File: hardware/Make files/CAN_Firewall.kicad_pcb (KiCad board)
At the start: 2 copper layers, 46.3 x 18.8 mm, 31 parts, among them IC1 ATXMEGA128A4U-M, J1 DB9, J2 DB9, U1 MCP2551-I/SN, U2 MCP2551-I/SN, U3 MC78M05CDT, U4 TLV70033DDC, U5 PESDxL5UY

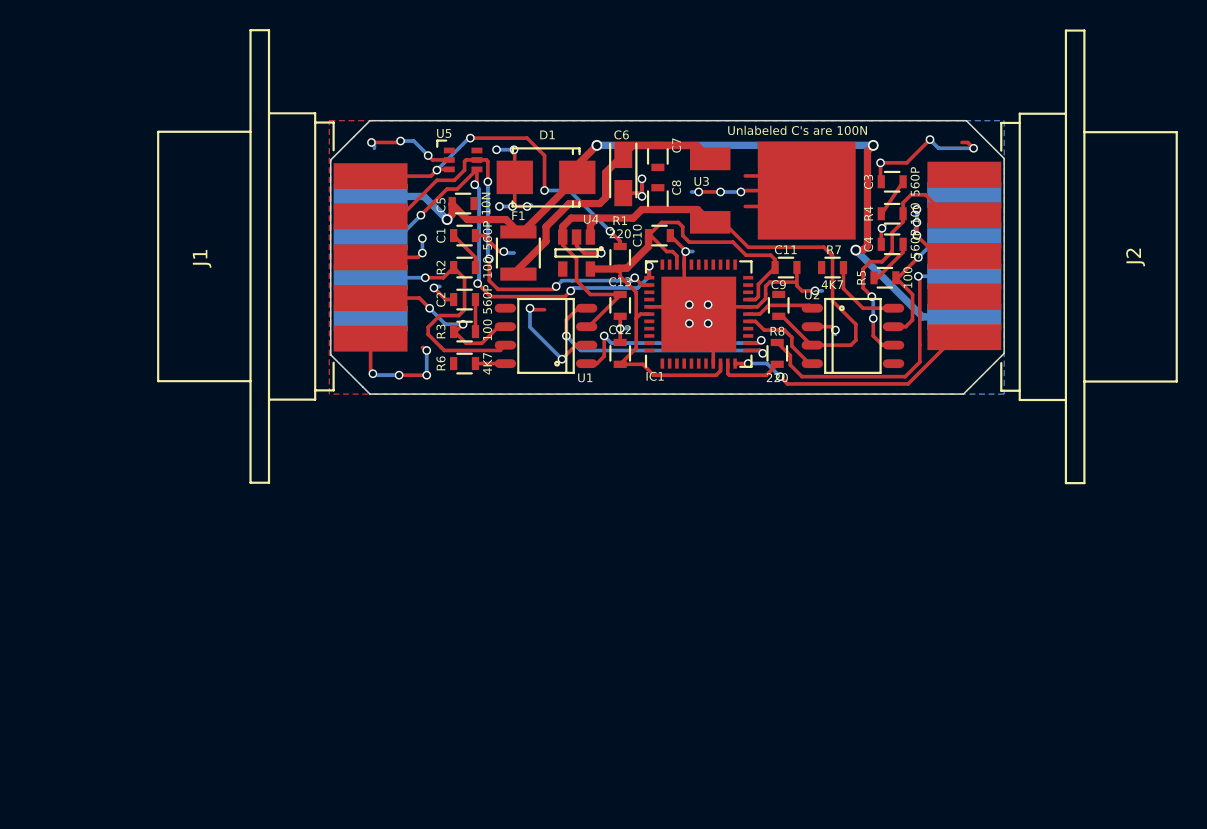
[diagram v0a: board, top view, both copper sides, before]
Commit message: V1.1 Devlopment
Created teh V1.1 hardware files. The Hardware patch for V1 will follow
this design.
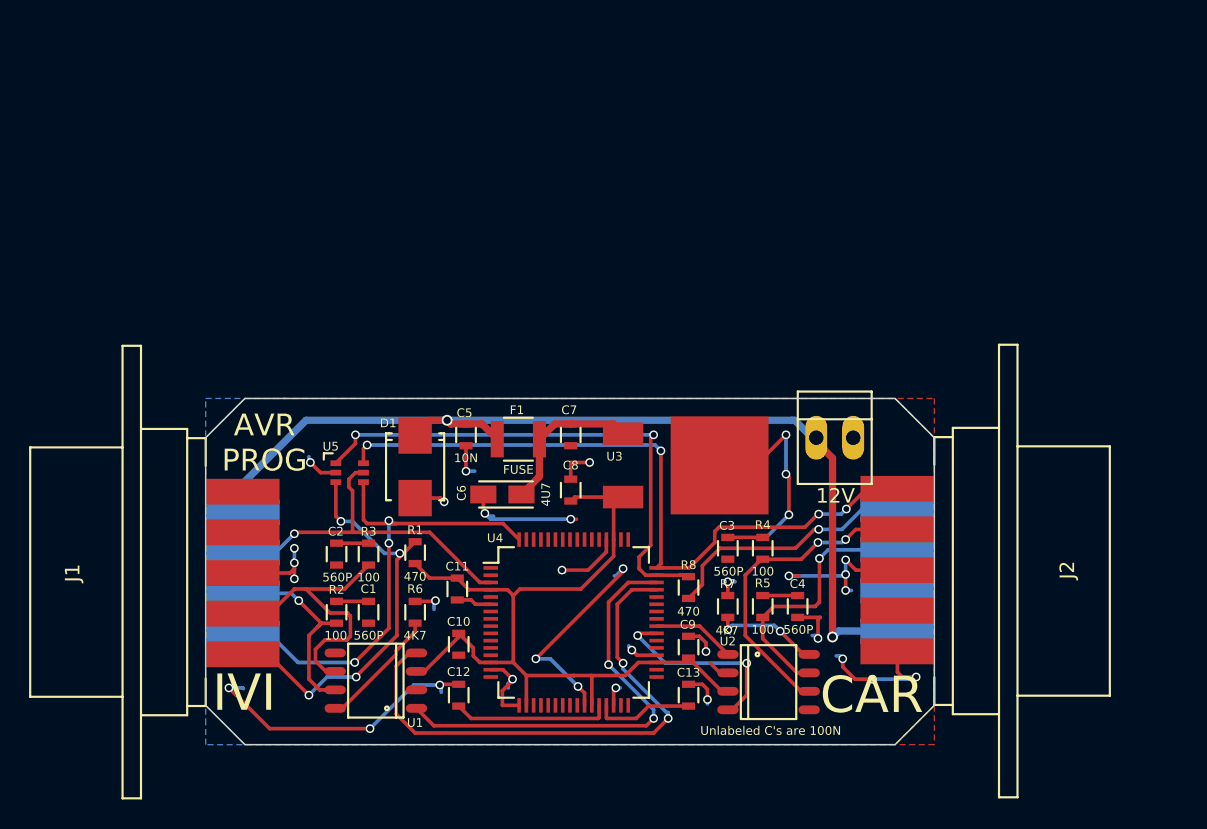
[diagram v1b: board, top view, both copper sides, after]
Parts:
- removed IC1: ATXMEGA128A4U-M, Housings_DFN_QFN:QFN-44-1EP_7x7mm_Pitch0.5mm
- added 12V: PINHEAD1-2, Connect:PINHEAD1-2, F.Cu at (96.5, 118.3)
- R1, R8: value 220 -> 470
- U4: value TLV70033DDC -> AT32UC3C; footprint Housings_SOT-23_SOT-143_TSOT-6:SOT-23-5 -> Housings_QFP:LQFP-64_10x10mm_Pitch0.5mm
- moved C11 31.6 mm to (70.6, 128.7), turned to 270 degrees
- moved C10 31.3 mm to (70.7, 132.5), turned to 270 degrees
- moved C3 27.6 mm to (89.2, 125.9), turned to 270 degrees
- moved C13 27.2 mm to (86.5, 136.0), turned to 90 degrees
- moved C1 26.7 mm to (64.5, 130.3), turned to 270 degrees
- moved U1 26.4 mm to (65.0, 135.0)
- moved C12 26.0 mm to (70.7, 136.0)
- moved C4 25.7 mm to (94.0, 129.9), turned to 270 degrees
- moved U4 25.4 mm to (78.6, 131.0), turned to 0 degrees
- moved R2 25.3 mm to (62.3, 130.3), turned to 90 degrees
- moved R1 24.7 mm to (67.7, 126.2)
- moved R4 24.7 mm to (91.6, 125.9), turned to 90 degrees
- moved U2 24.5 mm to (92.0, 135.1)
- moved R7 24.4 mm to (89.2, 129.9), turned to 90 degrees
- moved C9 24.3 mm to (86.5, 132.7)
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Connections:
- C10 pad 1: +3V3 -> +5V
- C11 pad 1: +3V3 -> +5V
- C12 pad 1: +3V3 -> Net-(C12-Pad1)
- C13 pad 1: +5V -> Net-(C13-Pad1)
- J1 pad 1: GND -> 5P
- J1 pad 4: ~RESET/PDI_CLK -> Net-(J1-Pad4)
- J1 pad 5: 3V3P -> GND
- J1 pad 6: Net-(J1-Pad6) -> ~RESET/A_DATA
- J1 pad 8: PDI_DATA -> A_DATAOUT
- J2 pad 1: Net-(J2-Pad1) -> LOOP_B
- J2 pad 5: LOOP_B -> GND
- R1 pad 1: +3V3 -> +5V
- R1 pad 2: 3V3P -> 5P
- R8 pad 1: Net-(J2-Pad8) -> Net-(J2-Pad6)
- U4 pad 1: +5V -> Net-(U4-Pad1)
- U4 pad 2: GND -> Net-(U4-Pad2)
- U4 pad 3: +5V -> A_DATAOUT
- U4 pad 4: (no net) -> +5V
- U4 pad 5: +3V3 -> (no net)
- U5 pad 1: Net-(U5-Pad1) -> LOOP_A
- U5 pad 3: 3V3P -> 5P
- U5 pad 4: PDI_DATA -> ~RESET/A_DATA
- U5 pad 5: ~RESET/PDI_CLK -> A_DATAOUT
- U5 pad 6: Net-(U5-Pad6) -> LOOP_B
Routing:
- net +3V3: track 39.2 -> 0.00 mm
- net ~RESET/A_DATA: track 0.00 -> 33.7 mm, vias 0 -> 3
- net LOOP_A: track 4.50 -> 36.3 mm, vias 0 -> 2
- net PDI_DATA: track 31.6 -> 0.00 mm, vias 5 -> 0
- net LOOP_B: track 17.7 -> 49.1 mm, vias 2 -> 4
- net ~RESET/PDI_CLK: track 30.1 -> 0.00 mm, vias 4 -> 0
- net 5P: track 0.00 -> 28.8 mm, vias 0 -> 4
- net A_DATAOUT: track 0.00 -> 25.9 mm, vias 0 -> 1
- net 3V3P: track 23.8 -> 0.00 mm, vias 4 -> 0
- net GND: track 103.2 -> 124.5 mm, vias 39 -> 34
- net RX0: track 17.9 -> 37.4 mm
- net Net-(J2-Pad8): track 20.7 -> 1.36 mm, vias 1 -> 0
- net Net-(J2-Pad6): track 0.00 -> 17.7 mm, vias 0 -> 1
- net TX0: track 14.9 -> 30.2 mm
- net +5V: track 45.3 -> 58.2 mm
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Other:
- board size 46.3 x 18.8 mm -> 50.1 x 23.8 mm
- board text added: "- + 12V"
- board text added: "AVR PROG"
- board text added: "CANBUS Firewall V1.1 Open Source Hardware Jaguar Land Rover OSTC Jesse Banks 2015"
- board text added: "CAR"
- board text added: "IVI"
- board text removed: "CANBUS Firewall V1.0 Open Source Hardware Jaguar Land Rover OSTC Jesse Banks 2015"

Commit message: V1.1 Diag port improved
added another resistor in the Loop B input, to facilitate a "bypass
mode" in conjunction with a "rule learn mode".
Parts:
- added R9: 470, Custom Parts:R_0603_sm, F.Cu at (71.2, 30.6)
- moved C1 98.0 mm to (41.6, 35.0)
- moved R2 98.0 mm to (39.5, 35.0)
- moved R6 98.0 mm to (44.9, 35.0)
- moved 12V 98.0 mm to (73.7, 23.1)
- moved C10 98.0 mm to (47.9, 37.2)
- moved C12 98.0 mm to (47.9, 40.8)
- moved C13 98.0 mm to (63.6, 40.8)
- moved C2 98.0 mm to (39.5, 31.1)
- moved C3 98.0 mm to (66.3, 30.6)
- moved C4 98.0 mm to (71.2, 34.6)
- moved C5 98.0 mm to (48.4, 22.9)
- moved C6 98.0 mm to (50.9, 26.9)
- moved C7 98.0 mm to (55.5, 22.9)
- moved C8 98.0 mm to (55.5, 26.6)
- moved D1 98.0 mm to (44.9, 25.1)
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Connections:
- J2 pad 1: LOOP_B -> Net-(J2-Pad1)
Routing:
- net GND: track 124.5 -> 156.9 mm, vias 34 -> 37
- net Net-(J2-Pad1): track 0.00 -> 11.0 mm, vias 0 -> 2
- net Net-(R7-Pad1): track 7.39 -> 16.3 mm, vias 2 -> 0
- net LOOP_B: track 49.1 -> 41.0 mm, vias 4 -> 2
- net CAR_CANL: track 21.9 -> 23.0 mm
- net CAR_CANH: track 18.6 -> 18.0 mm
